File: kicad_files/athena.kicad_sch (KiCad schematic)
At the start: 619 parts, among them J1 TYPE-C-31-M-12, J2 A1001WR-S-04P, Q1 2N7002, Q2 2N7002, Q3 AO3401A, Q4 2N7002, Q5 2N7002, Q6 2N7002, Q7 2N7002, Q8 2N7002, SW1 K2-1187SQ-A4SW-06, SW10 MX Switch, SW100 MX Switch, SW101 MX Switch, SW102 MX Switch, SW103 MX Switch, SW104 MX Switch, SW105 MX Switch, SW106 MX Switch, SW107 MX Switch, SW108 MX Switch, SW109 MX Switch, SW11 MX Switch, SW110 MX Switch, SW111 MX Switch, SW112 MX Switch, SW113 MX Switch, SW114 MX Switch, SW115 MX Switch, SW116 MX Switch, SW117 MX Switch, SW118 MX Switch, SW119 MX Switch, SW12 MX Switch, SW120 MX Switch, SW13 MX Switch, SW14 MX Switch, SW15 MX Switch, SW16 MX Switch, SW17 MX Switch, SW18 MX Switch, SW19 MX Switch, SW2 MX Switch, SW20 MX Switch, SW21 MX Switch, SW22 MX Switch, SW23 MX Switch, SW24 MX Switch, SW25 MX Switch, SW26 MX Switch, SW27 MX Switch, SW28 MX Switch, SW29 MX Switch, SW3 MX Switch, SW30 MX Switch, SW31 MX Switch, SW32 MX Switch, SW33 MX Switch, SW34 MX Switch, SW35 MX Switch, SW36 MX Switch, SW37 MX Switch, SW38 MX Switch, SW39 MX Switch, SW4 MX Switch, SW40 MX Switch, SW41 MX Switch, SW42 MX Switch, SW43 MX Switch, SW44 MX Switch, SW45 MX Switch, SW46 MX Switch, SW47 MX Switch, SW48 MX Switch, SW49 MX Switch, SW5 MX Switch, SW50 MX Switch, SW51 MX Switch, SW52 MX Switch, SW53 MX Switch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

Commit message: More DRC
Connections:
- net VBUS: now also FB3.2; no longer FB3.1
- net at F1.1: now also FB3.1; no longer FB3.2
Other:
- moved on the sheet: FB3
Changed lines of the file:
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@@
     )
   )
-  (symbol (lib_id "Device:FerriteBead") (at 482.6 107.95 90) (unit 1)
-    (in_bom yes) (on_board yes) (dnp no) (fields_autoplaced)
-    (property "Reference" "FB3" (at 482.5492 100.965 90)
+  (symbol (lib_id "Device:FerriteBead") (at 482.6 107.95 270) (mirror x) (unit 1)
+    (in_bom yes) (on_board yes) (dnp no)
+    (property "Reference" "FB3" (at 482.6508 100.965 90)
       (effects (font (size 1.27 1.27)))
     )
-    (property "Value" "4.7u" (at 482.5492 103.505 90)
+    (property "Value" "4.7u" (at 482.6508 103.505 90)
       (effects (font (size 1.27 1.27)))
     )

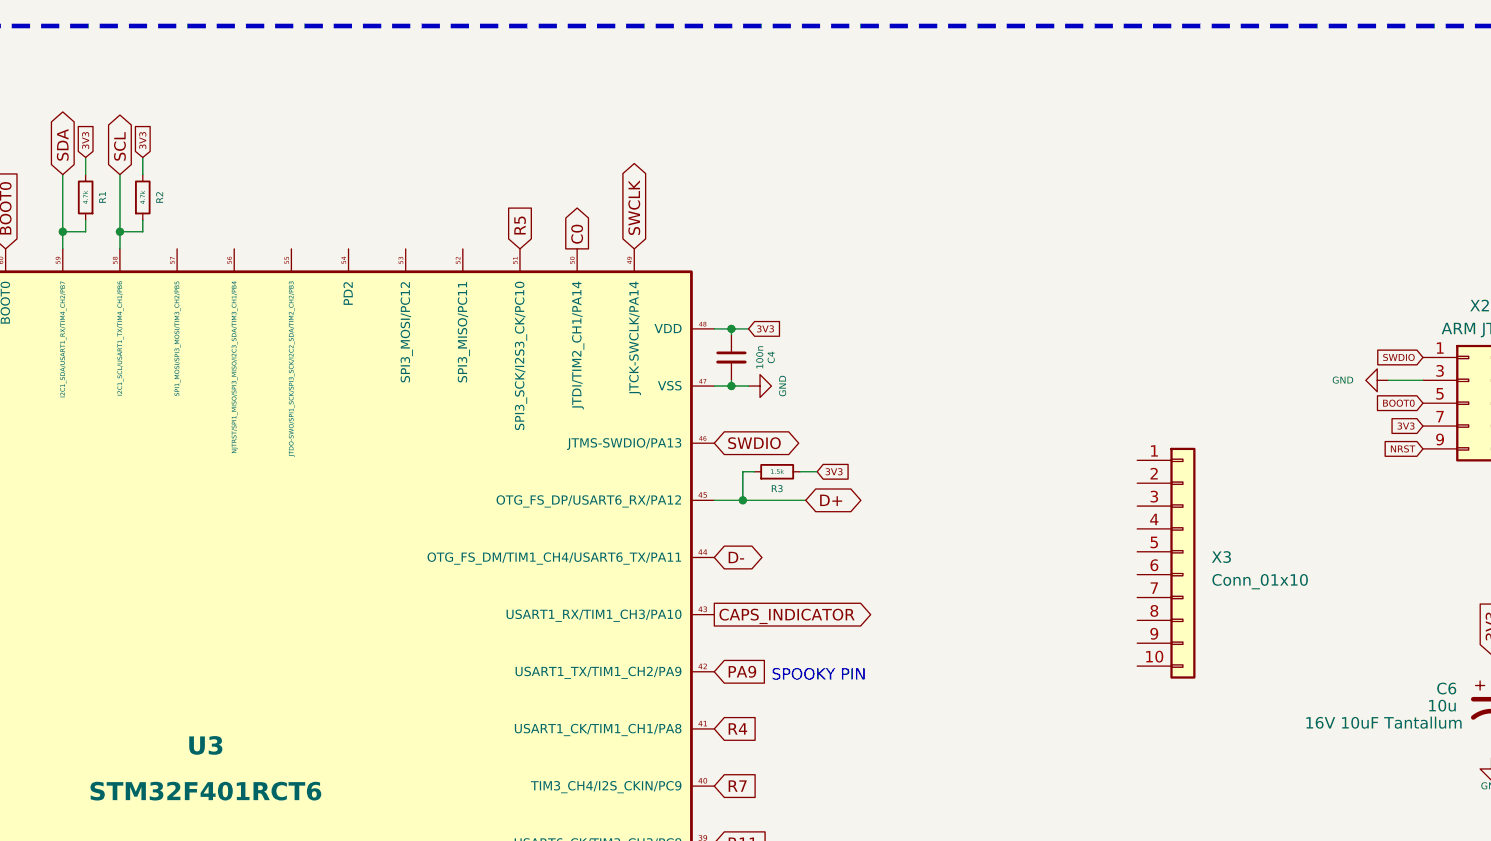
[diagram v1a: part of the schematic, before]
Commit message: Expose extra pins and power pins
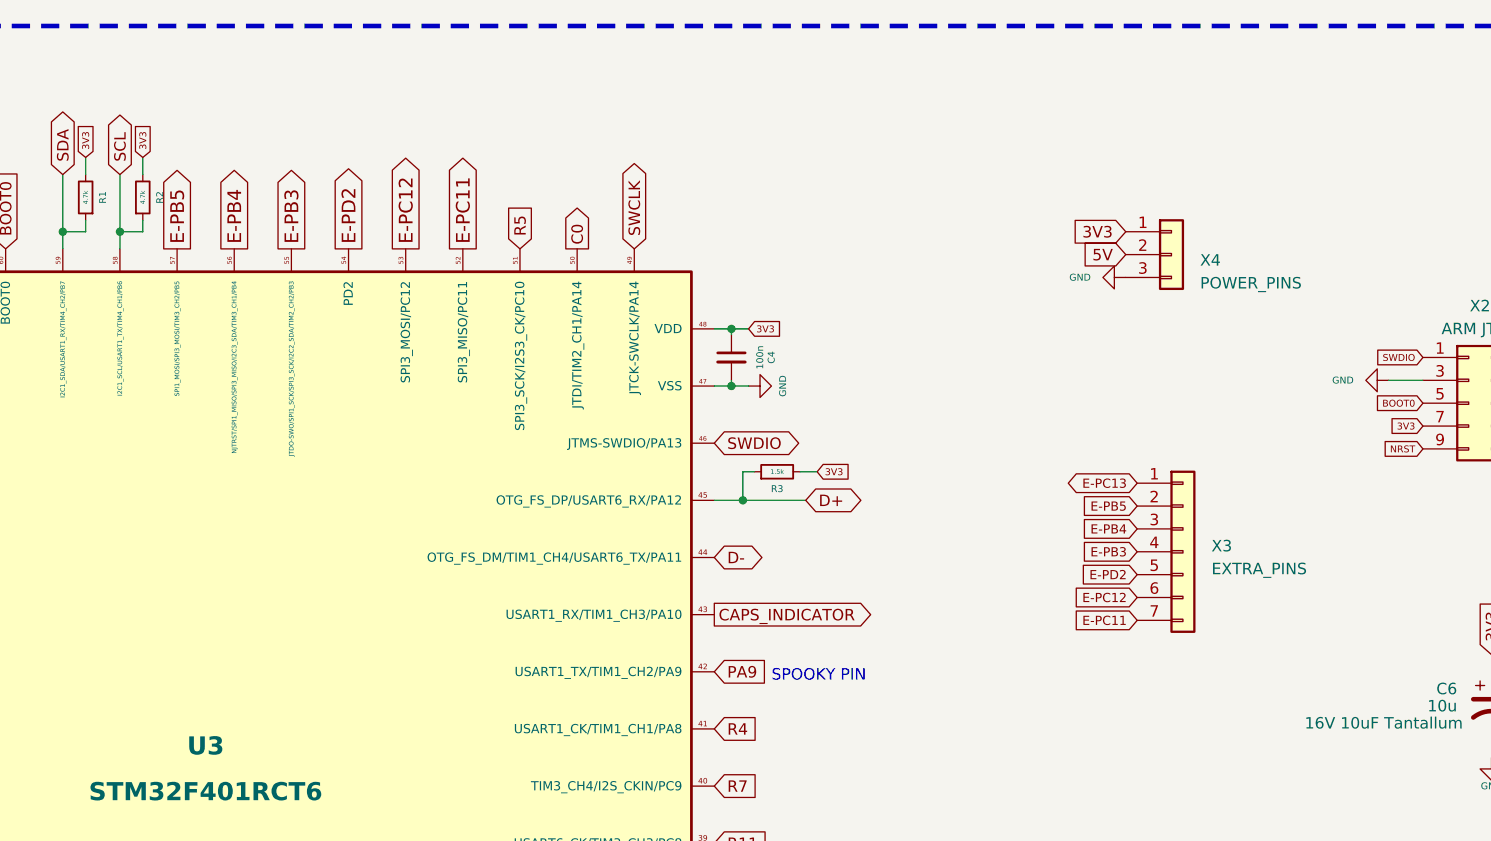
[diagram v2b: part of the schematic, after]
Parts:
- added X4: POWER_PINS, acheron_Connectors:PinHeader_1x3_staggered_P2.54mm_Vertical, symbol Connector_Generic:Conn_01x03
- X3: value Conn_01x10 -> EXTRA_PINS; footprint acheron_Connectors:PinHeader_1x10_P2.54mm_Vertical -> acheron_Connectors:PinHeader_1x7_P2.54mm_Vertical; symbol Connector_Generic:Conn_01x10 -> Connector_Generic:Conn_01x07; now in the parts list
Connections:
- net 3V3: now also X4.1 (Pin_1)
- net 5V: now also X4.2 (Pin_2)
- net E-PC13: now also X3.1 (Pin_1)
- net GND: now also X4.3 (Pin_3)
- net E-PC11: now reaches U3.52 (SPI3_MISO/PC11)
- net E-PC11: now also X3.7 (Pin_7)
- net E-PC12: now reaches U3.53 (SPI3_MOSI/PC12)
- net E-PC12: now also X3.6 (Pin_6)
- net E-PD2: now reaches U3.54 (PD2)
- net E-PD2: now also X3.5 (Pin_5)
- net E-PB3: now reaches U3.55 (JTDO-SWO/SPI1_SCK/SPI3_SCK/I2C2_SDA/TIM2_CH2/PB3)
- net E-PB3: now also X3.4 (Pin_4)
- net E-PB4: now reaches U3.56 (NJTRST/SPI1_MISO/SPI3_MISO/I2C3_SDA/TIM3_CH1/PB4)
- net E-PB4: now also X3.3 (Pin_3)
- net E-PB5: now reaches U3.57 (SPI1_MOSI/SPI3_MOSI/TIM3_CH2/PB5)
- net E-PB5: now also X3.2 (Pin_2)
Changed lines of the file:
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@@
     )
   )
+  (global_label "E-PC12" (shape output) (at 281.305 43.815 90)
+    (effects (font (size 1.524 1.524)) (justify left))
+    (property "Intersheetrefs" "${INTERSHEET_REFS}" (at 281.2574 40.2625 90)
+      (effects (font (size 1.524 1.524)) (justify left) hide)
+    )
+  )
   (global_label "R5" (shape input) (at 294.005 43.815 90)
     (effects (font (size 1.27 1.27)) (justify left))
@@
     )
   )
+  (global_label "E-PC13" (shape bidirectional) (at 362.585 69.85 180)
+    (effects (font (size 1.016 1.016)) (justify right))
+    (property "Intersheetrefs" "${INTERSHEET_REFS}" (at 359.0325 69.8976 0)
+      (effects (font (size 1.524 1.524)) (justify right) hide)
+    )
+  )
   (global_label "C10" (shape output) (at 249.555 156.845 270)
     (effects (font (size 1.27 1.27)) (justify right))
@@
     )
   )
+  (global_label "E-PD2" (shape input) (at 362.585 80.01 180)
+    (effects (font (size 1.016 1.016)) (justify right))
+    (property "Intersheetrefs" "${INTERSHEET_REFS}" (at 359.0325 80.0576 0)
+      (effects (font (size 1.524 1.524)) (justify right) hide)
+    )
+  )
   (global_label "5V" (shape input) (at 469.9 349.25 90)
     (effects (font (size 1.27 1.27)) (justify left))
@@
     )
   )
+  (global_label "E-PC11" (shape output) (at 287.655 43.815 90)
+    (effects (font (size 1.524 1.524)) (justify left))
+    (property "Intersheetrefs" "${INTERSHEET_REFS}" (at 287.6074 40.2625 90)
+      (effects (font (size 1.524 1.524)) (justify left) hide)
+    )
+  )
   (global_label "R1" (shape input) (at 57.15 539.75 180)
     (effects (font (size 1.27 1.27)) (justify right))
@@
     )
   )
+  (global_label "E-PB3" (shape input) (at 362.585 77.47 180)
+    (effects (font (size 1.016 1.016)) (justify right))
+    (property "Intersheetrefs" "${INTERSHEET_REFS}" (at 359.0325 77.5176 0)
+      (effects (font (size 1.524 1.524)) (justify right) hide)
+    )
+  )
   (global_label "C6" (shape output) (at 274.955 156.845 270)
     (effects (font (size 1.27 1.27)) (justify right))
@@
     )
   )
+  (global_label "5V" (shape input) (at 361.315 44.45 180)
+    (effects (font (size 1.27 1.27)) (justify right))
+    (property "Intersheetrefs" "${INTERSHEET_REFS}" (at -276.86 -24.13 0)
+      (effects (font (size 1.27 1.27)) hide)
+    )
+  )
   (global_label "R9" (shape input) (at 57.15 844.55 180)
     (effects (font (size 1.27 1.27)) (justify right))
@@
     )
   )
+  (global_label "E-PC11" (shape input) (at 362.585 85.09 180)
+    (effects (font (size 1.016 1.016)) (justify right))
+    (property "Intersheetrefs" "${INTERSHEET_REFS}" (at 359.0325 85.1376 0)
+      (effects (font (size 1.524 1.524)) (justify right) hide)
+    )
+  )
   (global_label "C2" (shape input) (at 120.65 488.95 90)
     (effects (font (size 1.27 1.27)) (justify left))
@@
     )
   )
+  (global_label "E-PB4" (shape input) (at 362.585 74.93 180)
+    (effects (font (size 1.016 1.016)) (justify right))
+    (property "Intersheetrefs" "${INTERSHEET_REFS}" (at 359.0325 74.9776 0)
+      (effects (font (size 1.524 1.524)) (justify right) hide)
+    )
+  )
   (global_label "XTAL_OUT" (shape output) (at 201.295 84.455 180)
     (effects (font (size 1.27 1.27)) (justify right))
@@
     )
   )
+  (global_label "E-PB5" (shape input) (at 362.585 72.39 180)
+    (effects (font (size 1.016 1.016)) (justify right))
+    (property "Intersheetrefs" "${INTERSHEET_REFS}" (at 359.0325 72.4376 0)
+      (effects (font (size 1.524 1.524)) (justify right) hide)
+    )
+  )
   (global_label "PB2{slash}BOOT1" (shape output) (at 281.305 156.845 270)
     (effects (font (size 1.27 1.27)) (justify right))
@@
     )
   )
+  (global_label "E-PB3" (shape output) (at 268.605 43.815 90)
+    (effects (font (size 1.524 1.524)) (justify left))
+    (property "Intersheetrefs" "${INTERSHEET_REFS}" (at 268.5574 40.2625 90)
+      (effects (font (size 1.524 1.524)) (justify left) hide)
+    )
+  )
   (global_label "5V" (shape input) (at 342.9 400.05 90)
     (effects (font (size 1.27 1.27)) (justify left))
@@
     )
   )
+  (global_label "E-PC12" (shape input) (at 362.585 82.55 180)
+    (effects (font (size 1.016 1.016)) (justify right))
+    (property "Intersheetrefs" "${INTERSHEET_REFS}" (at 359.0325 82.5976 0)
+      (effects (font (size 1.524 1.524)) (justify right) hide)
+    )
+  )
   (global_label "R10" (shape input) (at 202.565 103.505 180)
     (effects (font (size 1.27 1.27)) (justify right))
@@
     )
   )
+  (global_label "3V3" (shape input) (at 361.315 41.91 180)
+    (effects (font (size 1.27 1.27)) (justify right))
+    (property "Intersheetrefs" "${INTERSHEET_REFS}" (at -276.86 -26.67 0)
+      (effects (font (size 1.27 1.27)) hide)
+    )
+  )
   (global_label "R3" (shape input) (at 57.15 615.95 180)
     (effects (font (size 1.27 1.27)) (justify right))
@@
     )
   )
+  (global_label "E-PB5" (shape output) (at 255.905 43.815 90)
+    (effects (font (size 1.524 1.524)) (justify left))
+    (property "Intersheetrefs" "${INTERSHEET_REFS}" (at 255.8574 40.2625 90)
+      (effects (font (size 1.524 1.524)) (justify left) hide)
+    )
+  )
+  (global_label "E-PD2" (shape output) (at 274.955 43.815 90)
+    (effects (font (size 1.524 1.524)) (justify left))
+    (property "Intersheetrefs" "${INTERSHEET_REFS}" (at 274.9074 40.2625 90)
+      (effects (font (size 1.524 1.524)) (justify left) hide)
+    )
+  )
   (global_label "C6" (shape input) (at 222.25 488.95 90)
     (effects (font (size 1.27 1.27)) (justify left))
@@
     )
   )
+  (global_label "E-PB4" (shape output) (at 262.255 43.815 90)
+    (effects (font (size 1.524 1.524)) (justify left))
+    (property "Intersheetrefs" "${INTERSHEET_REFS}" (at 262.2074 40.2625 90)
+      (effects (font (size 1.524 1.524)) (justify left) hide)
+    )
+  )
   (global_label "CAPS_INDICATOR" (shape output) (at 315.595 84.455 0)
     (effects (font (size 1.27 1.27)) (justify left))
@@
     )
   )
+  (symbol (lib_id "Connector_Generic:Conn_01x03") (at 366.395 44.45 0) (unit 1)
+    (in_bom yes) (on_board yes) (dnp no) (fields_autoplaced)
+    (property "Reference" "X4" (at 369.57 45.085 0)
+      (effects (font (size 1.27 1.27)) (justify left))
+    )
+    (property "Value" "POWER_PINS" (at 369.57 47.625 0)
+      (effects (font (size 1.27 1.27)) (justify left))
+    )
+    (property "Footprint" "acheron_Connectors:PinHeader_1x3_staggered_P2.54mm_Vertical" (at 366.395 44.45 0)
+      (effects (font (size 1.27 1.27)) hide)
+    )
+    (property "Datasheet" "~" (at 366.395 44.45 0)
+      (effects (font (size 1.27 1.27)) hide)
+    )
+    (property "Package" "" (at 366.395 44.45 0)
+      (effects (font (size 1.27 1.27)) hide)
+    )
+    (property "Manufacturer" "" (at 366.395 44.45 0)
+      (effects (font (size 1.27 1.27)) hide)
+    )
+    (property "Manufacturer Part Number" "" (at 366.395 44.45 0)
+      (effects (font (size 1.27 1.27)) hide)
+    )
+    (property "Vendor Part Number" "" (at 366.395 44.45 0)
+      (effects (font (size 1.27 1.27)) hide)
+    )
+    (property "Specification" "" (at 366.395 44.45 0)
+      (effects (font (size 1.27 1.27)) hide)
+    )
+    (pin "1")
+    (pin "2")
+    (pin "3")
+    (instances
+      (project "athena"
+        (path "/9ce6b20d-0a6c-402a-b232-5eafd6242eb3"
+          (reference "X4") (unit 1)
+        )
+      )
+    )
+  )
   (symbol (lib_id "Device:Ferrite_Bead_Small") (at 52.705 184.15 0) (unit 1)
     (in_bom yes) (on_board yes) (dnp no)
@@
     )
   )
+  (symbol (lib_id "power:GND") (at 361.315 46.99 270) (unit 1)
+    (in_bom yes) (on_board yes) (dnp no)
+    (property "Reference" "#PWR072" (at 354.965 46.99 0)
+      (effects (font (size 1.27 1.27)) hide)
+    )
+    (property "Value" "GND" (at 356.235 46.99 90)
+      (effects (font (size 0.762 0.762)))
+    )
+    (property "Footprint" "" (at 361.315 46.99 0)
+      (effects (font (size 1.27 1.27)) hide)
+    )
+    (property "Datasheet" "" (at 361.315 46.99 0)
+      (effects (font (size 1.27 1.27)) hide)
+    )
+    (pin "1")
+    (instances
+      (project "athena"
+        (path "/9ce6b20d-0a6c-402a-b232-5eafd6242eb3"
+          (reference "#PWR072") (unit 1)
+        )
+      )
+    )
+  )
   (symbol (lib_id "Device:D") (at 438.15 662.94 270) (unit 1)
     (in_bom yes) (on_board yes) (dnp no)
@@
     )
   )
-  (symbol (lib_id "Connector_Generic:Conn_01x10") (at 367.665 77.47 0) (unit 1)
-    (in_bom no) (on_board yes) (dnp no) (fields_autoplaced)
-    (property "Reference" "X3" (at 370.84 78.105 0)
+  (symbol (lib_id "Connector_Generic:Conn_01x07") (at 367.665 77.47 0) (unit 1)
+    (in_bom yes) (on_board yes) (dnp no) (fields_autoplaced)
+    (property "Reference" "X3" (at 370.84 76.835 0)
       (effects (font (size 1.27 1.27)) (justify left))
     )
-    (property "Value" "Conn_01x10" (at 370.84 80.645 0)
+    (property "Value" "EXTRA_PINS" (at 370.84 79.375 0)
       (effects (font (size 1.27 1.27)) (justify left))
     )
-    (property "Footprint" "acheron_Connectors:PinHeader_1x10_P2.54mm_Vertical" (at 367.665 77.47 0)
+    (property "Footprint" "acheron_Connectors:PinHeader_1x7_P2.54mm_Vertical" (at 367.665 77.47 0)
       (effects (font (size 1.27 1.27)) hide)
     )
@@
     )
     (pin "1")
-    (pin "10")
     (pin "2")
     (pin "3")
@@
     (pin "6")
     (pin "7")
-    (pin "8")
-    (pin "9")
     (instances
       (project "athena"

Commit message: First DRC test, some rerouting
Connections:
- net C0: now also U3.52 (SPI3_MISO/PC11); no longer U3.50 (JTDI/TIM2_CH1/PA14)
- net C14: now also U3.50 (JTDI/TIM2_CH1/PA14)
- net PA9: now also X3.7 (Pin_7)
- net R3: now also U3.51 (SPI3_SCK/I2S3_CK/PC10)
- net R5: now also U3.53 (SPI3_MOSI/PC12); no longer U3.51 (SPI3_SCK/I2S3_CK/PC10)
- net E-PB13: now reaches U3.34 (SPI2_SCK/I2S2_CK/PB13)
- net E-PB13: now also X3.6 (Pin_6)
- removed net E-PC11: U3.52 (SPI3_MISO/PC11), X3.7 (Pin_7)
- removed net E-PC12: U3.53 (SPI3_MOSI/PC12), X3.6 (Pin_6)
- no-connect marks 3 -> 2
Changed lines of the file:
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@@
   (junction (at 400.05 565.15) (diameter 1.016) (color 0 0 0 0)
   )
-  (no_connect (at 315.595 141.605))
   (no_connect (at 58.42 161.29))
   (no_connect (at 58.42 158.75))
@@
     )
   )
-  (global_label "E-PC12" (shape output) (at 281.305 43.815 90)
-    (effects (font (size 1.524 1.524)) (justify left))
-    (property "Intersheetrefs" "${INTERSHEET_REFS}" (at 281.2574 40.2625 90)
-      (effects (font (size 1.524 1.524)) (justify left) hide)
-    )
-  )
-  (global_label "R5" (shape input) (at 294.005 43.815 90)
+  (global_label "R5" (shape input) (at 281.305 43.815 90)
     (effects (font (size 1.27 1.27)) (justify left))
-    (property "Intersheetrefs" "${INTERSHEET_REFS}" (at 294.0844 36.6243 90)
+    (property "Intersheetrefs" "${INTERSHEET_REFS}" (at 281.3844 36.6243 90)
       (effects (font (size 1.27 1.27)) (justify left) hide)
     )
@@
     )
   )
+  (global_label "E-PB13" (shape input) (at 362.585 82.55 180)
+    (effects (font (size 1.016 1.016)) (justify right))
+    (property "Intersheetrefs" "${INTERSHEET_REFS}" (at 359.0325 82.5976 0)
+      (effects (font (size 1.524 1.524)) (justify right) hide)
+    )
+  )
   (global_label "R11" (shape input) (at 315.595 109.855 0)
     (effects (font (size 1.27 1.27)) (justify left))
@@
     )
   )
-  (global_label "E-PC11" (shape output) (at 287.655 43.815 90)
-    (effects (font (size 1.524 1.524)) (justify left))
-    (property "Intersheetrefs" "${INTERSHEET_REFS}" (at 287.6074 40.2625 90)
-      (effects (font (size 1.524 1.524)) (justify left) hide)
-    )
-  )
   (global_label "R1" (shape input) (at 57.15 539.75 180)
     (effects (font (size 1.27 1.27)) (justify right))
@@
     )
   )
-  (global_label "E-PC11" (shape input) (at 362.585 85.09 180)
-    (effects (font (size 1.016 1.016)) (justify right))
-    (property "Intersheetrefs" "${INTERSHEET_REFS}" (at 359.0325 85.1376 0)
-      (effects (font (size 1.524 1.524)) (justify right) hide)
-    )
-  )
   (global_label "C2" (shape input) (at 120.65 488.95 90)
     (effects (font (size 1.27 1.27)) (justify left))
@@
     )
   )
+  (global_label "PA9" (shape input) (at 362.585 85.09 180)
+    (effects (font (size 1.016 1.016)) (justify right))
+    (property "Intersheetrefs" "${INTERSHEET_REFS}" (at 357.6924 85.0106 0)
+      (effects (font (size 1.27 1.27)) (justify right) hide)
+    )
+  )
   (global_label "NRST" (shape output) (at 654.05 107.95 0)
     (effects (font (size 1.27 1.27)) (justify left))
@@
     )
   )
+  (global_label "C14" (shape output) (at 300.355 43.815 90)
+    (effects (font (size 1.27 1.27)) (justify left))
+    (property "Intersheetrefs" "${INTERSHEET_REFS}" (at -86.995 -15.24 0)
+      (effects (font (size 1.27 1.27)) (justify left) hide)
+    )
+  )
   (global_label "RGB_5V_MAIN" (shape output) (at 613.41 263.525 0)
     (effects (font (size 1.27 1.27)) (justify left))
@@
     )
   )
-  (global_label "E-PC12" (shape input) (at 362.585 82.55 180)
-    (effects (font (size 1.016 1.016)) (justify right))
-    (property "Intersheetrefs" "${INTERSHEET_REFS}" (at 359.0325 82.5976 0)
-      (effects (font (size 1.524 1.524)) (justify right) hide)
-    )
-  )
   (global_label "R10" (shape input) (at 202.565 103.505 180)
     (effects (font (size 1.27 1.27)) (justify right))
@@
     )
   )
+  (global_label "E-PB13" (shape output) (at 315.595 141.605 0)
+    (effects (font (size 1.524 1.524)) (justify left))
+    (property "Intersheetrefs" "${INTERSHEET_REFS}" (at 319.1475 141.5574 0)
+      (effects (font (size 1.524 1.524)) (justify left) hide)
+    )
+  )
   (global_label "R8" (shape input) (at 315.595 135.255 0)
     (effects (font (size 1.27 1.27)) (justify left))
@@
     )
   )
-  (global_label "C0" (shape output) (at 300.355 43.815 90)
+  (global_label "C0" (shape output) (at 287.655 43.815 90)
     (effects (font (size 1.27 1.27)) (justify left))
-    (property "Intersheetrefs" "${INTERSHEET_REFS}" (at -86.995 -15.24 0)
+    (property "Intersheetrefs" "${INTERSHEET_REFS}" (at -99.695 -15.24 0)
       (effects (font (size 1.27 1.27)) (justify left) hide)
     )
@@
     )
   )
+  (global_label "R3" (shape input) (at 294.005 43.815 90)
+    (effects (font (size 1.27 1.27)) (justify left))
+    (property "Intersheetrefs" "${INTERSHEET_REFS}" (at 294.0844 36.6243 90)
+      (effects (font (size 1.27 1.27)) (justify left) hide)
+    )
+  )
